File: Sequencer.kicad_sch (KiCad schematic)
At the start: 5 parts, among them J201 Seq Relay control, U201 LM2901, U202 ULN2004A

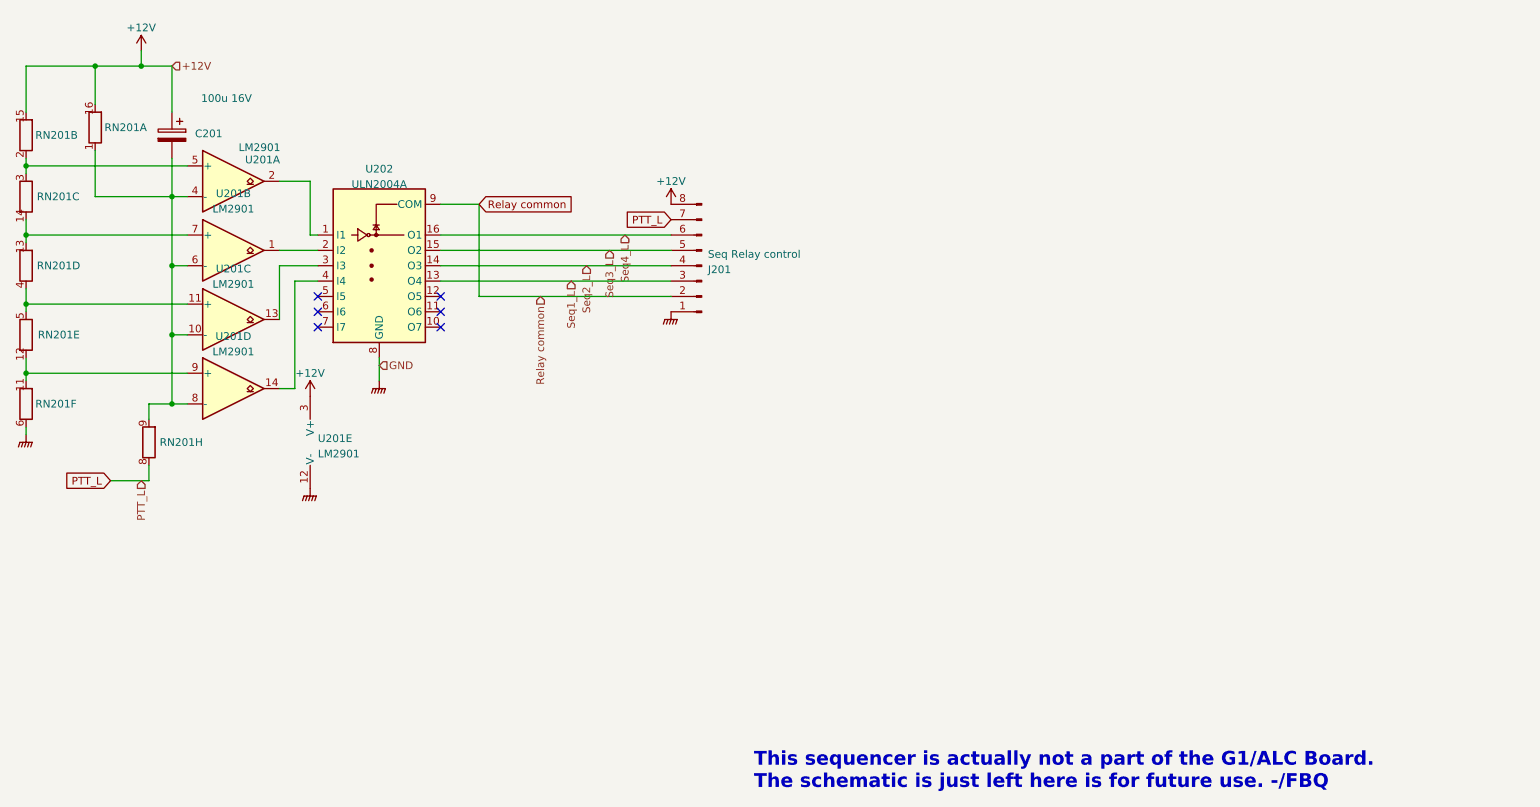
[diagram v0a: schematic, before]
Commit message: The outputs of the comparators needed pullup resistors. Which have been added. This makes the ERV checker happier.
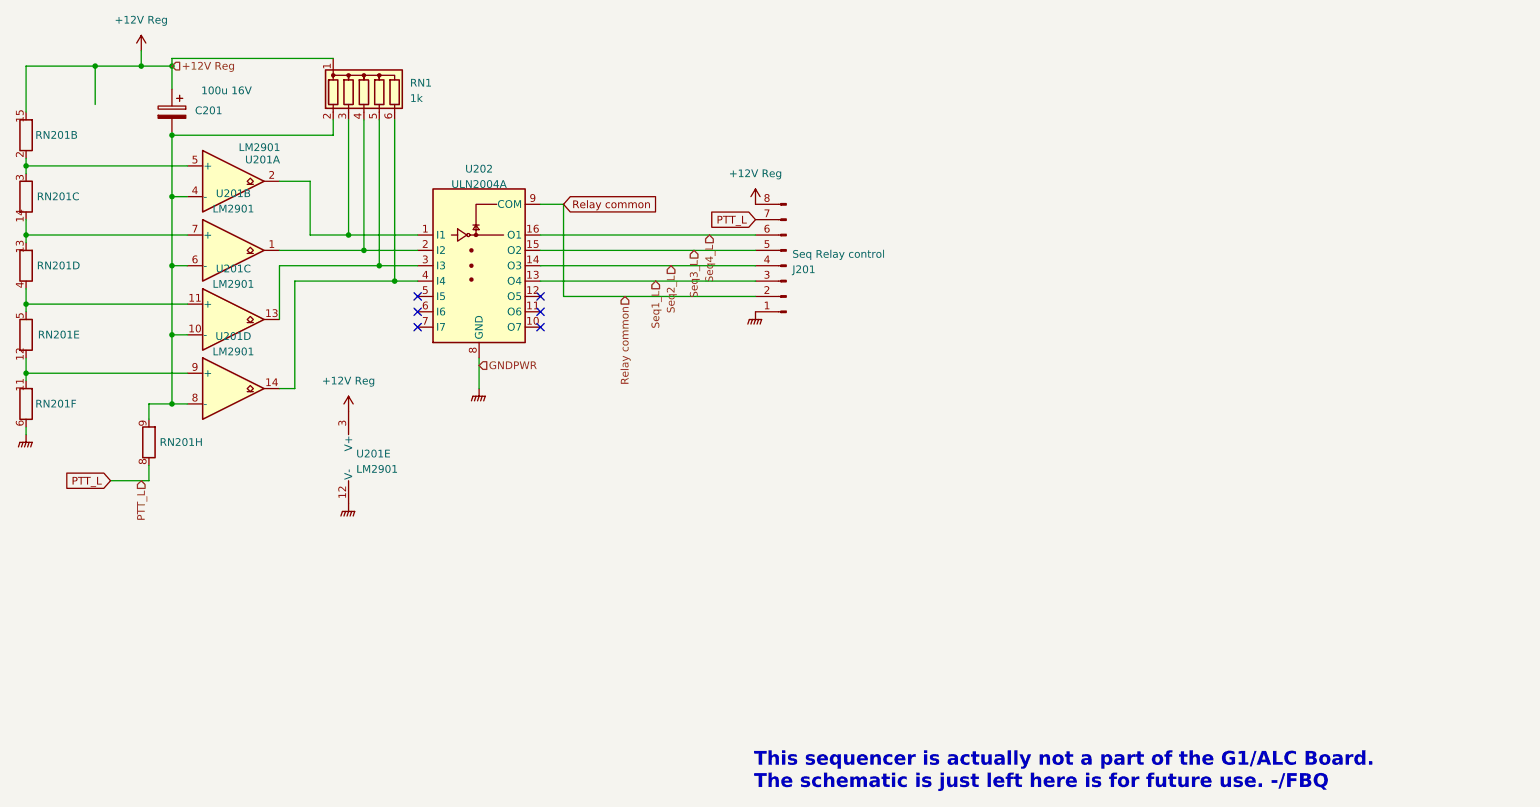
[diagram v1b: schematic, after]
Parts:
- removed unit 1 of RN201
- added RN1: 1k, Resistor_THT:R_Array_SIP6, symbol Device:R_Network05
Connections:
- net at C201.2, RN201.9 (R8.2), U201.10 (-)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: now also RN1.2 (R1)
- net at U201.14, U202.4 (I4): now also RN1.6 (R5)
- net at U201.2, U202.1 (I1): now also RN1.3 (R2)
- net at U201.1, U202.2 (I2): now also RN1.4 (R3)
- net at U201.13, U202.3 (I3): now also RN1.5 (R4)
- net +12V renamed +12V Reg
- net +12V Reg: now also RN1.1 (common)
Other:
- moved on the sheet: C201, J201, U201E, U202

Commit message: Updated format to KiCad 9. Included footprints etc.
Standardized PCB layers, updated property formatting, and adjusted net assignments. Added some DigiKey, Electrokit, and Mouser component part numbers.
Reduced font sizes for better readability and incorporated embedded font settings.
Removed the sequencer from the schematic which wasn't really meant to be there.
Revised and excluded drc and erc warnings and exclusions.
Included footprints into the project library that formerly was defined outside of the project.
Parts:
- C?: renamed from C201; Electrokit # (none) -> 41013566; Electrokit SEK (none) -> Electrokit; Order # 41013566 -> (none); Supplier Electrokit -> (none)
- J?: renamed from J201; Electrokit # (none) -> 40210033; Electrokit SEK (none) -> Electrokit; Order # 40210033 -> (none); Supplier Electrokit -> (none)
- U? (x5): renamed from U201; Electrokit # (none) -> 31-LM2901QS14-13CT-ND; Electrokit SEK (none) -> DigiKey; Order # 31-LM2901QS14-13CT-ND -> (none); Supplier DigiKey -> (none)
- U?: renamed from U202; Electrokit # (none) -> 296-15067-1-ND; Electrokit SEK (none) -> DigiKey; Order # 296-15067-1-ND -> (none); Supplier DigiKey -> (none)
- renumbered RN201 to RN?, RN1 to RN?
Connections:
- net +12V Reg renamed +12V
- net GNDPWR renamed GND
